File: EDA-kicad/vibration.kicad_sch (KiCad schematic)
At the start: 4 parts

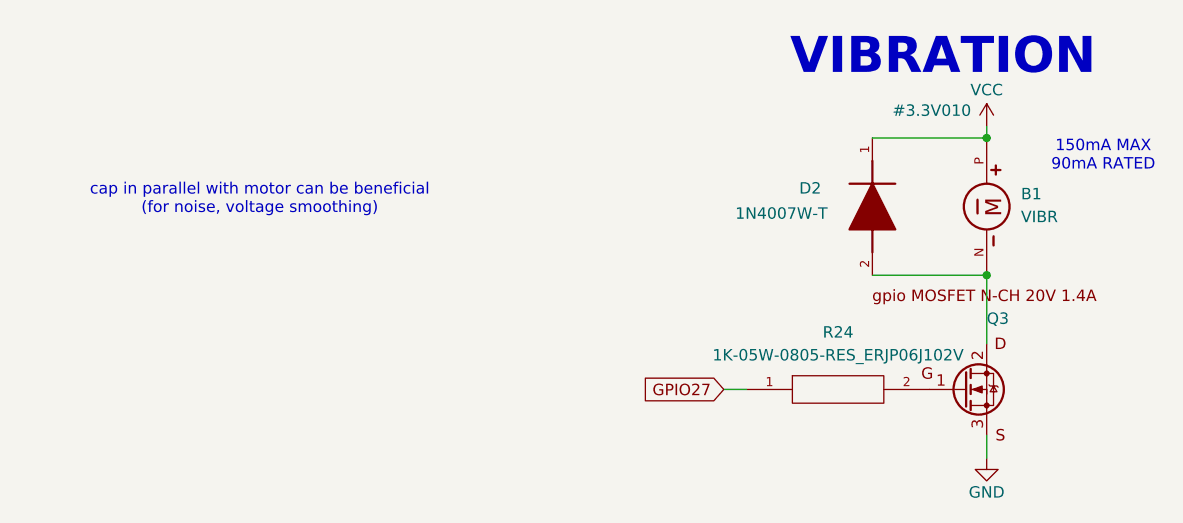
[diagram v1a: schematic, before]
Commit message: set everything except from power to DNP
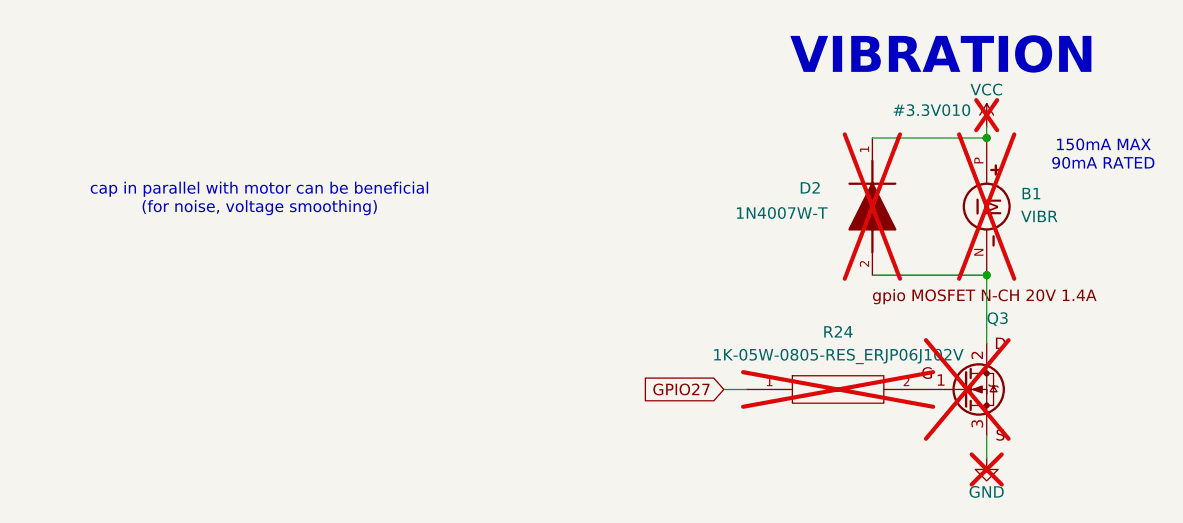
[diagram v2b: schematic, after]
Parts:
- B1, D2, Q3, R24: now not fitted

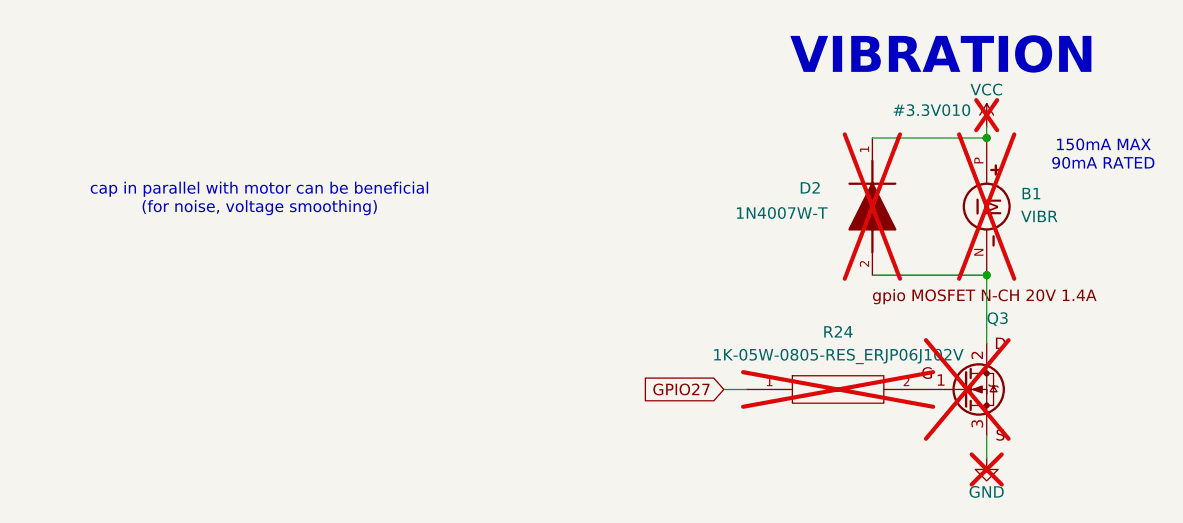
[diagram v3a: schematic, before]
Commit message: Improve KiCAD schematic design and labeling
- Replace overused global labels with hierarchical and local labels
- Add proper GND connections to components
- Fix BACKLIGHT- net issues
- Apply minor schematic fixes and cleanups
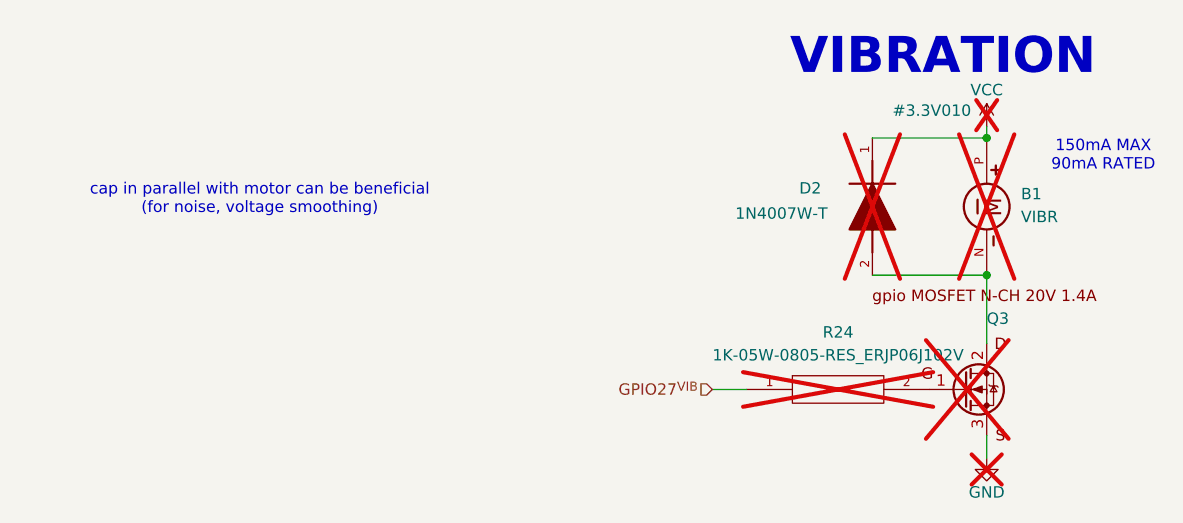
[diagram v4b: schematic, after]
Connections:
- net GPIO27 renamed GPIO27^{VIB}
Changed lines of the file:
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@@
 	(wire
 		(pts
-			(xy 147.32 110.49) (xy 149.86 110.49)
+			(xy 146.05 110.49) (xy 149.86 110.49)
 		)
 		(stroke
@@
 	)
 	(image
-		(at 118.618 93.726)
+		(at 135.128 61.976)
 		(data "iVBORw0KGgoAAAANSUhEUgAAAagAAAGYCAIAAACYquE6AAAAA3NCSVQICAjb4U/gAAAgAElEQVR4"
 			"nOydd5wU1dKG3zqTNrBklpwkSlCCICAIApIkCYISBAMYQT9zwMhVFEFMYESCklFEoiJxkSw5Sc4Z"
@@
 		)
 	)
-	(global_label "GPIO27"
+	(hierarchical_label "GPIO27^{VIB}"
 		(shape input)
-		(at 147.32 110.49 180)
-		(fields_autoplaced yes)
+		(at 146.05 110.49 180)
 		(effects
 			(font
@@
 			(justify right)
 		)
-		(property "Intersheetrefs" "${INTERSHEET_REFS}"
-			(at 137.4405 110.49 0)
-			(effects
-				(font
-					(size 1.27 1.27)
-				)
-				(justify right)
-				(hide yes)
-			)
-		)
 	)
